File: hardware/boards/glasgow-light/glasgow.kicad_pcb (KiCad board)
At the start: 2 copper layers, 171 parts, among them J1 USB_C_USB2.0, J10 AUX, J2 IDC-Header_2x5_P2.54mm, J3 IDC-Header_2x5_P2.54mm, J4 Conn_01x02, U10 SN74LVC1T45DCKR, U11 SN74LVC1T45DCKR, U12 INA180A2, U15 TPD3S014, U16 SN74LVC1T45DCKR, U17 SN74LVC1T45DCKR, U18 SN74LVC1T45DCKR, U19 PCA6408APW, U31 TPS73101DBV, U36 TLV73312PQDRVR, U4 SN74LVC1T45DCKR, U5 ICE40UP5K-SG48ITR, U6 SN74LVC1T45DCKR, U7 GD32VF103, U8 TLV75533PDRVR, U9 SN74LVC1T45DCKR, Y1 8M

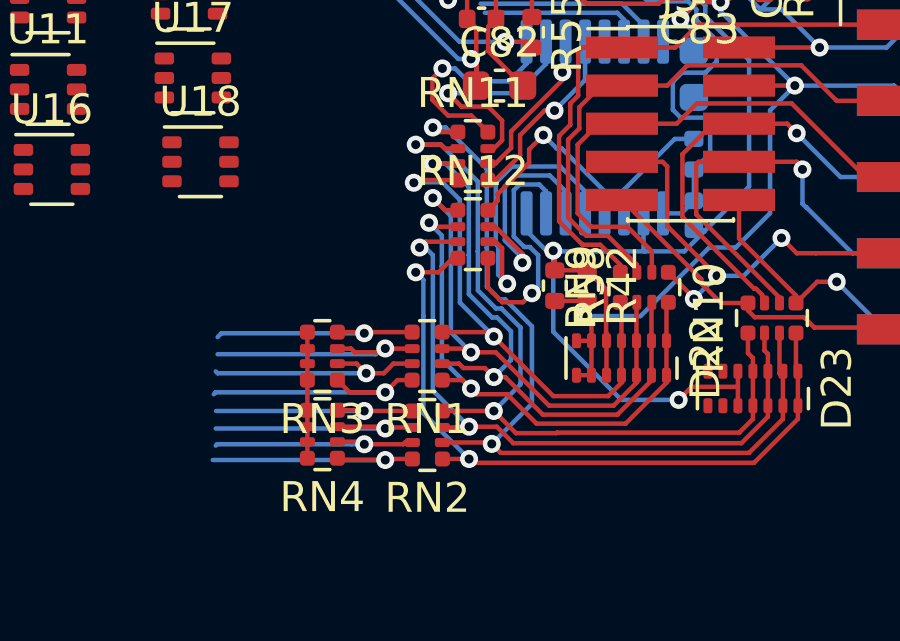
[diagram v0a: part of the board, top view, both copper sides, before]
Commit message: swap some pins
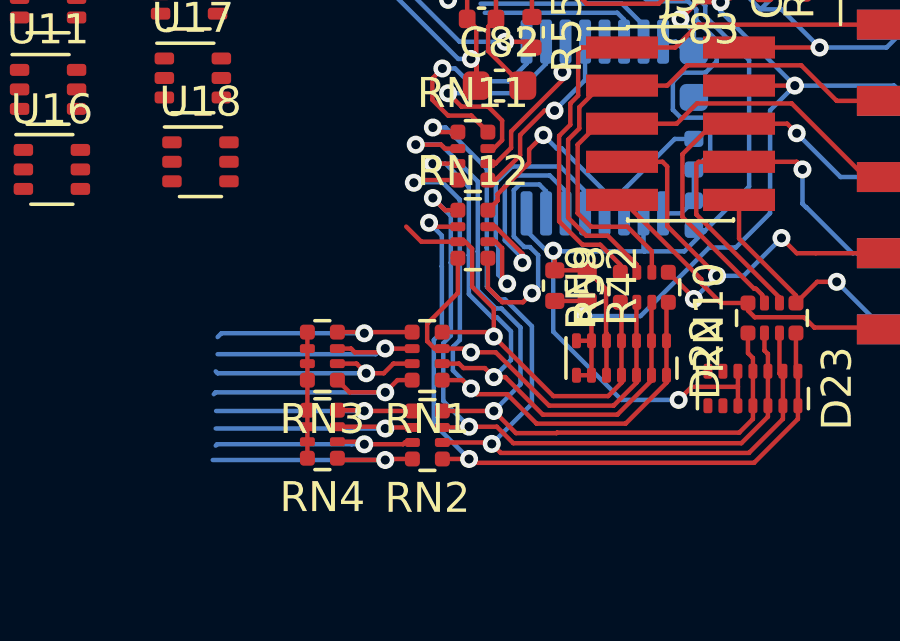
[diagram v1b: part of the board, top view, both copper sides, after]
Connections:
- RN11 pad 4: /IO_Banks/IO_Buffer_A/Y0 -> /IO_Banks/IO_Buffer_A/Y3
- RN12 pad 1: /IO_Banks/IO_Buffer_A/Y1 -> /IO_Banks/IO_Buffer_A/Y5
- RN12 pad 2: /IO_Banks/IO_Buffer_A/Y3 -> /IO_Banks/IO_Buffer_A/Y7
- RN12 pad 3: /IO_Banks/IO_Buffer_A/Y5 -> /IO_Banks/IO_Buffer_A/Y0
- RN12 pad 4: /IO_Banks/IO_Buffer_A/Y7 -> /IO_Banks/IO_Buffer_A/Y1
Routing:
- net /IO_Banks/IO_Buffer_A/Y3: track 18.4 -> 21.2 mm
- net /IO_Banks/IO_Buffer_A/Y1: track 16.9 -> 14.2 mm, vias 2 -> 1
- net /IO_Banks/IO_Buffer_A/Y0: track 18.2 -> 15.7 mm, vias 2 -> 1
- net /IO_Banks/IO_Buffer_A/Y5: track 22.4 -> 23.6 mm
- net /IO_Banks/IO_Buffer_A/Y7: track 24.0 -> 25.1 mm

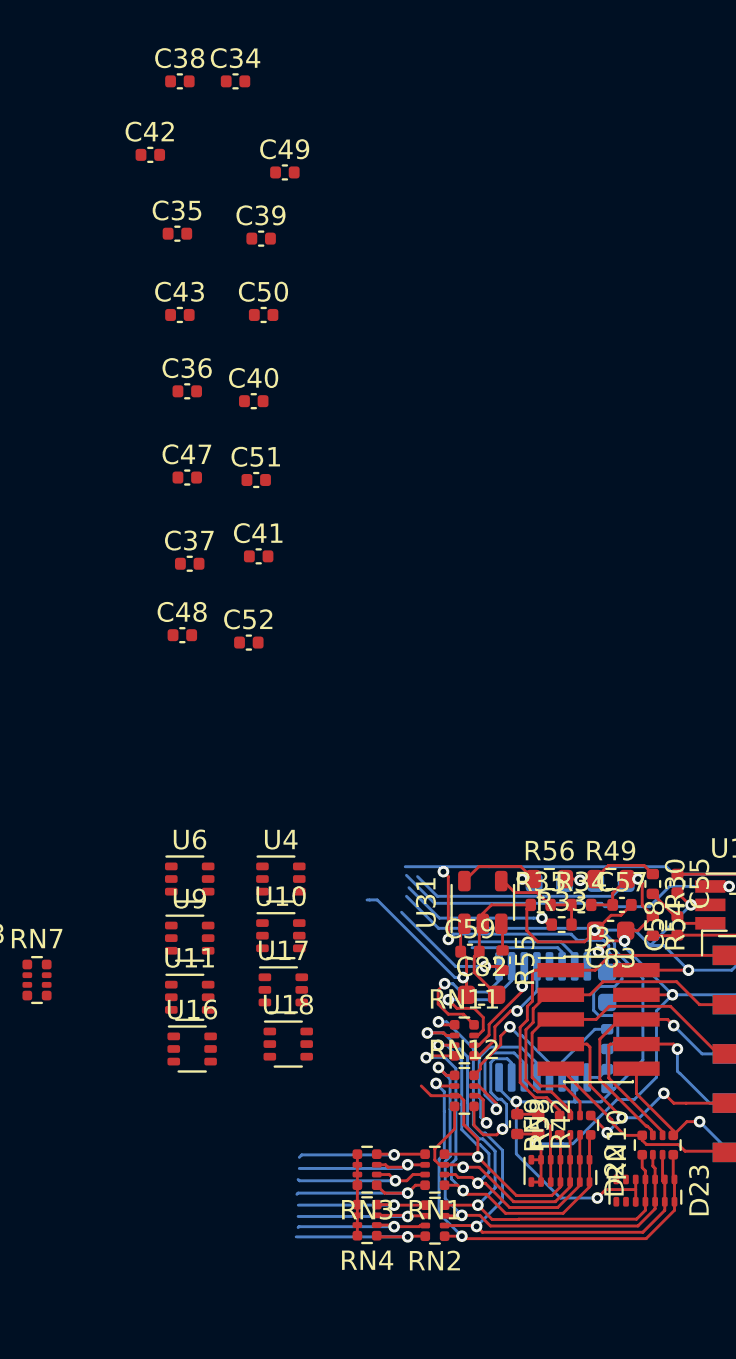
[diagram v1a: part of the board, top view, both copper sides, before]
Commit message: place&route the buffers
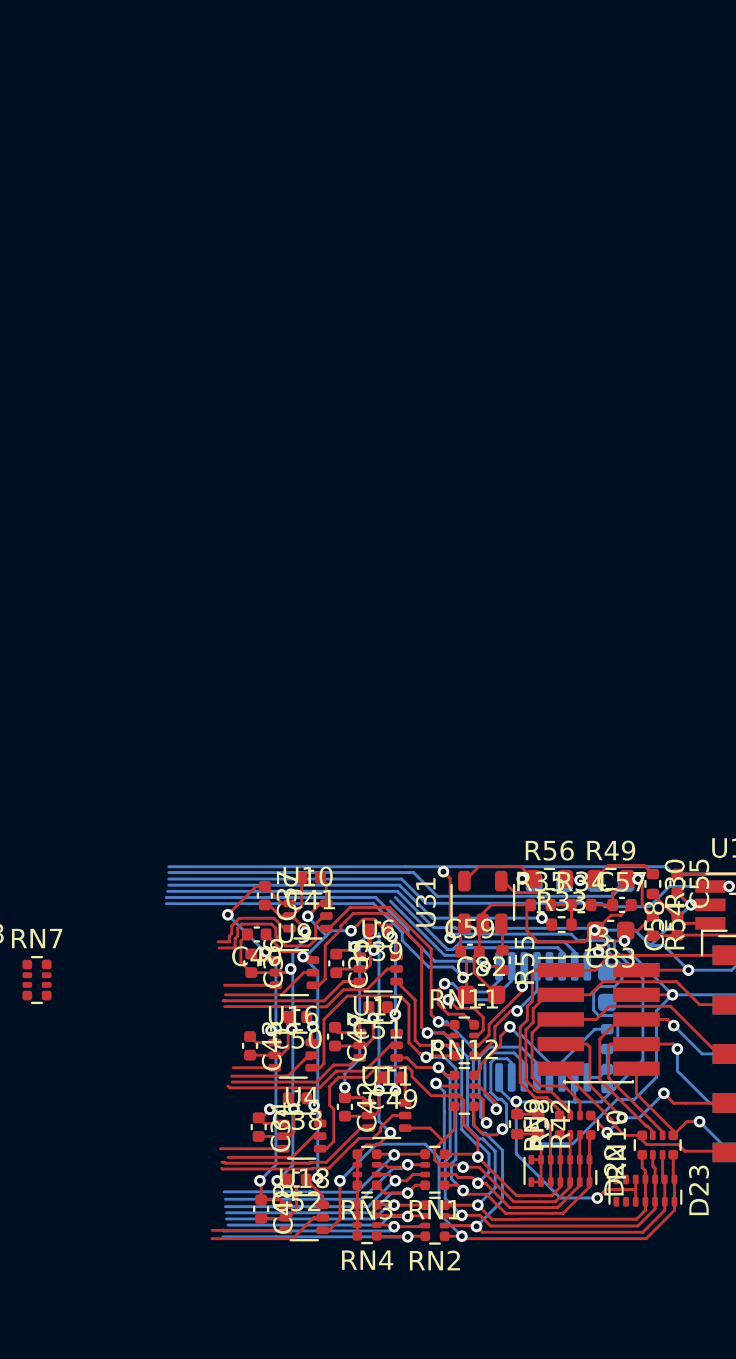
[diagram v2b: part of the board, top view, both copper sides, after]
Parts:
- moved C34 53.9 mm to (146.8, 47.8), turned to 270 degrees
- moved C38 52.8 mm to (148.8, 46.4), turned to 180 degrees
- moved C42 50.1 mm to (151.3, 46.8), turned to 270 degrees
- moved C49 47.0 mm to (153.7, 45.3), turned to 180 degrees
- moved C35 38.5 mm to (150.8, 39.4), turned to 270 degrees
- moved C43 37.9 mm to (146.4, 43.7), turned to 270 degrees
- moved C50 36.2 mm to (148.8, 42.2), turned to 180 degrees
- moved C39 36.1 mm to (153.0, 37.7), turned to 180 degrees
- moved C48 29.9 mm to (146.9, 52.1), turned to 270 degrees
- moved C47 29.8 mm to (150.7, 43.2), turned to 270 degrees
- moved C36 29.7 mm to (146.4, 39.4), turned to 270 degrees
- moved C51 27.9 mm to (153.0, 41.7), turned to 180 degrees
- moved C52 27.8 mm to (148.8, 50.5), turned to 180 degrees
- moved C40 27.5 mm to (146.7, 37.9), turned to 180 degrees
- moved C37 17.5 mm to (147.1, 35.9), turned to 270 degrees
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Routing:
- net GND: track 83.9 -> 157.8 mm, vias 5 -> 14
- net /IO_Banks/VIOA: track 50.5 -> 109.1 mm, vias 5 -> 14
- net +3V3: track 44.9 -> 100.8 mm, vias 3 -> 11
- net /IO_Banks/IO_Buffer_A/Y4: track 26.5 -> 40.1 mm
- net VIO_ENA: track 6.44 -> 19.0 mm
- net VIO_DAC: track 8.15 -> 20.6 mm
- net VIO_CURRENT: track 18.7 -> 30.9 mm
- net /IO_Banks/IO_Buffer_A/Y3: track 21.2 -> 32.4 mm
- net /IO_Banks/IO_Buffer_A/Y6: track 28.6 -> 39.4 mm
- net /IO_Banks/DA1: track 0.00 -> 10.7 mm
- net +5V: track 11.4 -> 22.0 mm
- net /IO_Banks/DA2: track 0.00 -> 9.67 mm
- net /IO_Banks/IO_Buffer_A/Y0: track 15.7 -> 25.3 mm
- net /IO_Banks/DA5: track 0.00 -> 9.52 mm
- net /IO_Banks/IO_Buffer_A/Y7: track 25.1 -> 34.4 mm, vias 2 -> 3
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
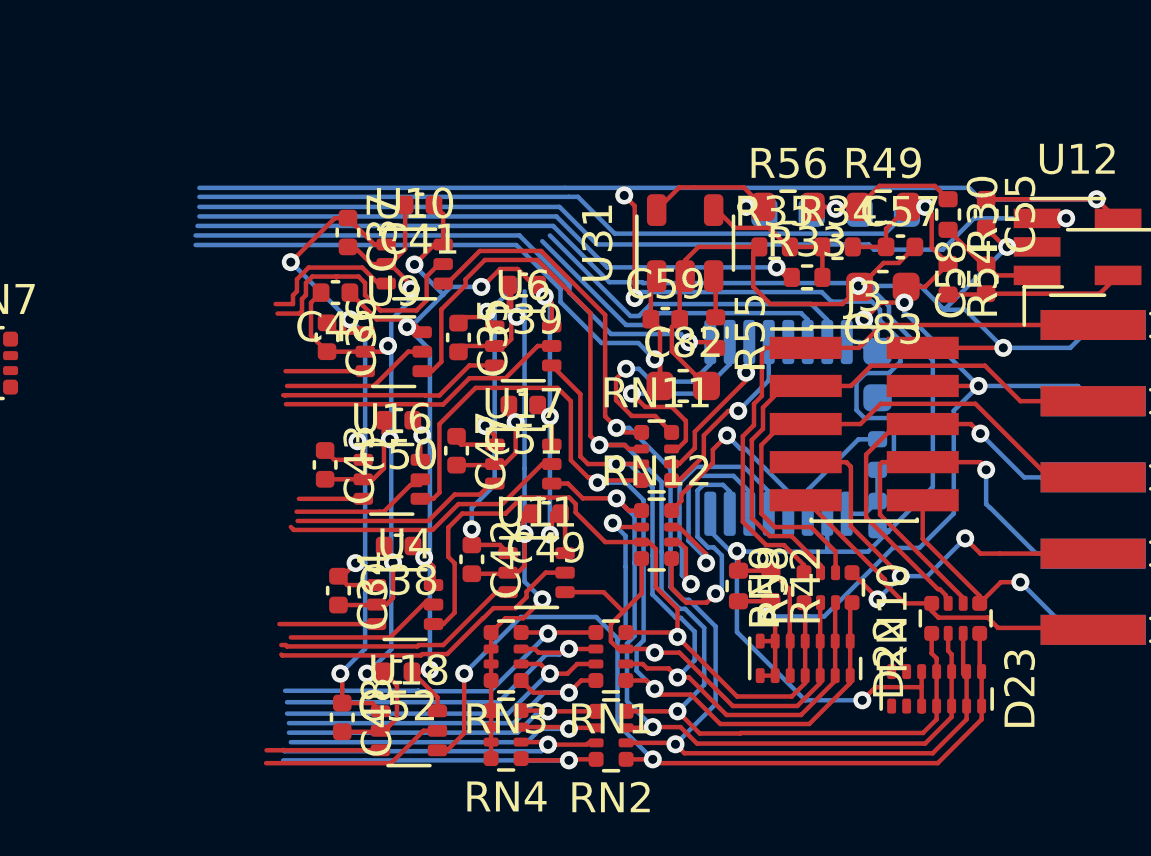
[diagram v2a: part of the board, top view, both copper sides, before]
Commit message: fix routing problems near the buffers
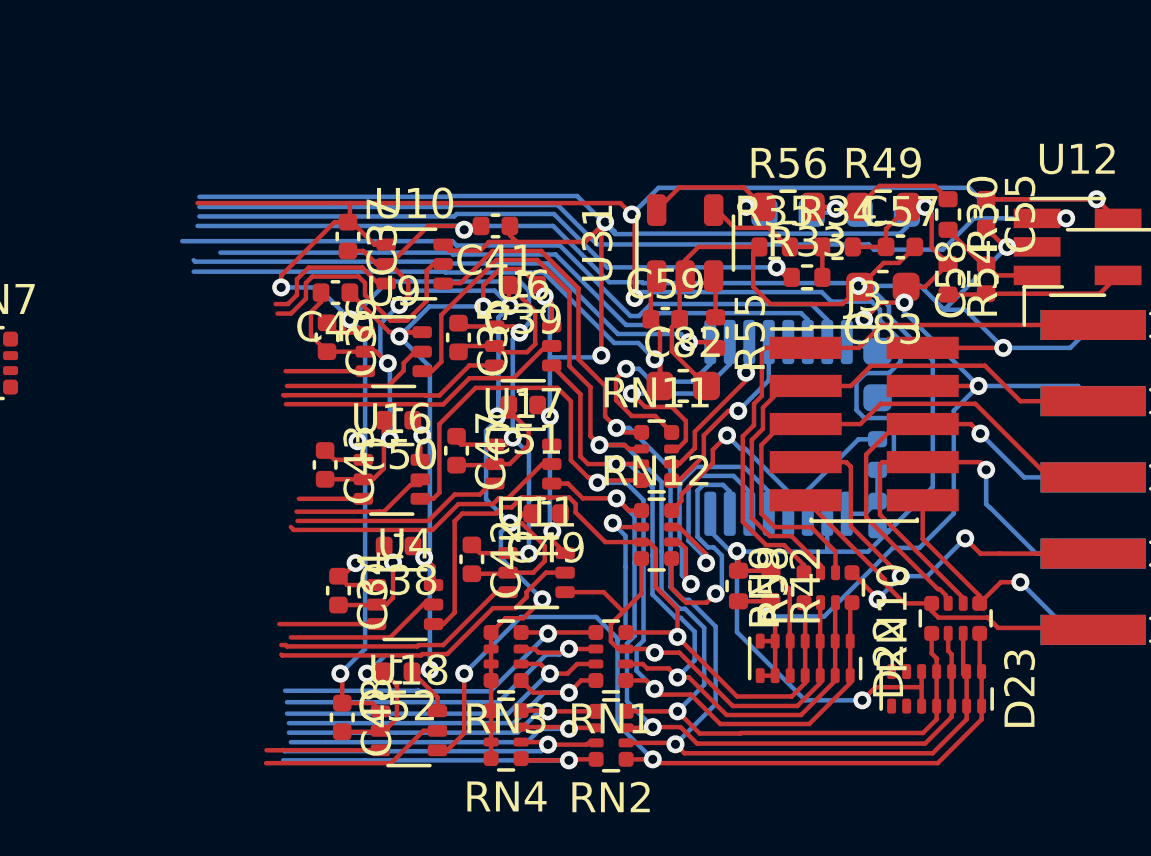
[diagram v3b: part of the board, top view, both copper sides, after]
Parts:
- moved C41 2.63 mm to (152.0, 35.7)
- moved C37 0.13 mm to (147.1, 36.0)
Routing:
- net /SDA: track 11.5 -> 23.7 mm
- net /SCL: track 11.0 -> 21.6 mm
- net /IO_Banks/VIOA: track 109.1 -> 119.3 mm, vias 14 -> 15
- net +3V3: track 100.8 -> 109.2 mm
- net GND: track 157.8 -> 161.6 mm, vias 14 -> 15
- net Net-(R30-Pad1): track 5.04 -> 6.74 mm
- net Net-(R56-Pad1): track 4.71 -> 5.40 mm
- net +5V: track 22.0 -> 21.4 mm

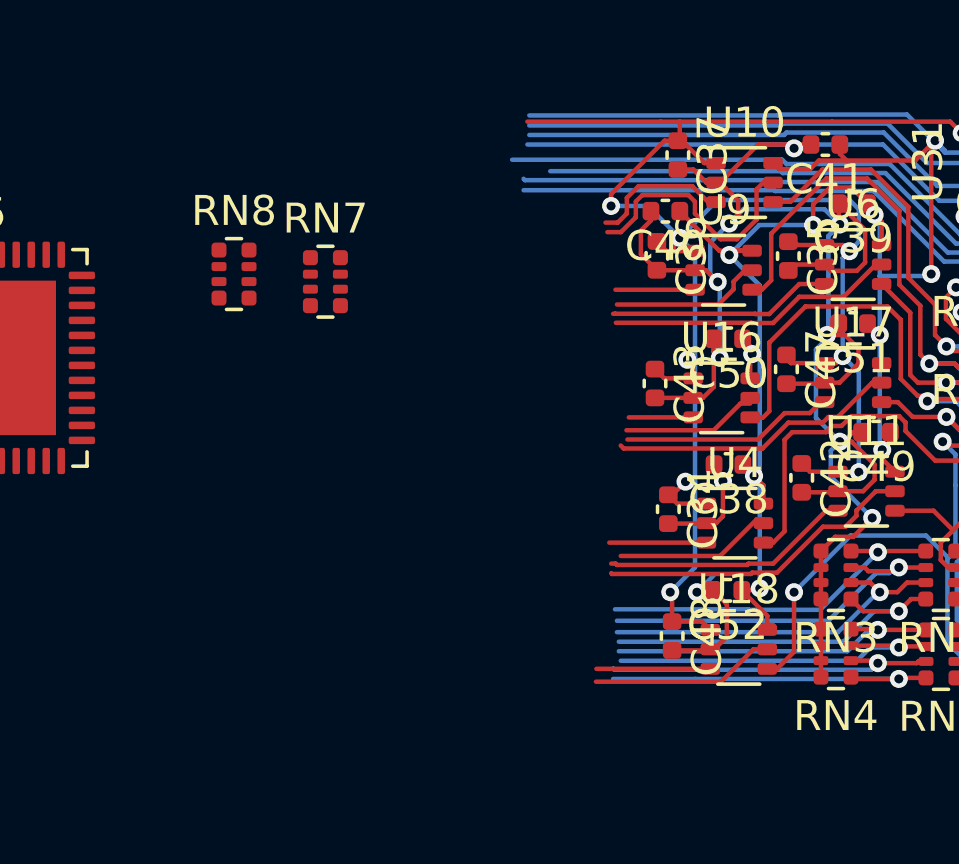
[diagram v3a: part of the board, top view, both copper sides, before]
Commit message: route resistor arrays between FPGA and buffers
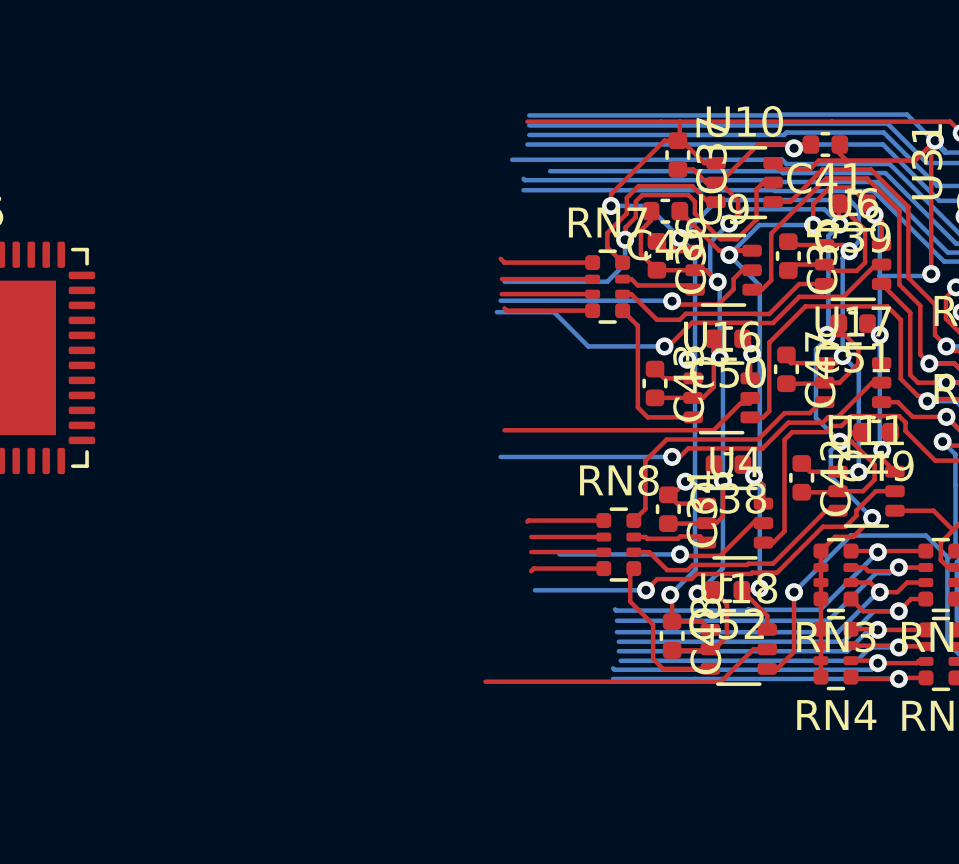
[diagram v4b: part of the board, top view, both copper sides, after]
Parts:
- moved RN8 15.7 mm to (145.2, 49.0)
- moved RN7 9.41 mm to (144.8, 40.4)
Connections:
- U10 pad 3: Net-(RN8-Pad6) -> /IO_Banks/IO_Buffer_A/X0
- U11 pad 3: Net-(RN7-Pad7) -> Net-(RN8-Pad6)
- U17 pad 3: Net-(RN8-Pad7) -> Net-(RN8-Pad8)
- U4 pad 3: /IO_Banks/IO_Buffer_A/X0 -> Net-(RN8-Pad7)
- U9 pad 3: Net-(RN8-Pad8) -> Net-(RN7-Pad7)
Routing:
- net GND: track 161.6 -> 169.1 mm
- net Net-(RN8-Pad8): track 2.65 -> 8.81 mm
- net Net-(RN7-Pad7): track 8.33 -> 2.56 mm
- net /IO_Banks/DA6: track 8.56 -> 13.4 mm, vias 0 -> 1
- net /IO_Banks/DA2: track 9.67 -> 14.4 mm, vias 0 -> 1
- net Net-(RN8-Pad7): track 6.96 -> 2.56 mm
- net /IO_Banks/DA5: track 9.52 -> 13.6 mm, vias 0 -> 1
- net /IO_Banks/DA3: track 4.49 -> 8.56 mm
- net /IO_Banks/DA4: track 5.13 -> 9.11 mm, vias 0 -> 1
- net /IO_Banks/DA7: track 6.16 -> 9.84 mm
- net Net-(RN7-Pad5): track 2.15 -> 5.42 mm
- net Net-(RN8-Pad6): track 4.72 -> 7.87 mm
- net /IO_Banks/QA0: track 0.00 -> 3.12 mm
- net /IO_Banks/QA2: track 0.00 -> 3.03 mm
- net /IO_Banks/QA1: track 0.00 -> 3.02 mm
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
